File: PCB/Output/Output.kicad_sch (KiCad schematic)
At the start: 44 parts, among them J1 USB-C, J10 O8, J11 O9, J12 O10, J2 POWER, J3 O1, J4 O2, J5 O3, J6 O4, J7 O5, J8 O6, J9 O7, U1 ESP32-PICO-MINI-02, U10 QR, U11 CH340X, U3 ISL89410, U4 ISL89410, U5 ISL89410, U6 ISL89410, U7 ISL89410, U8 MD8942, U9 AA

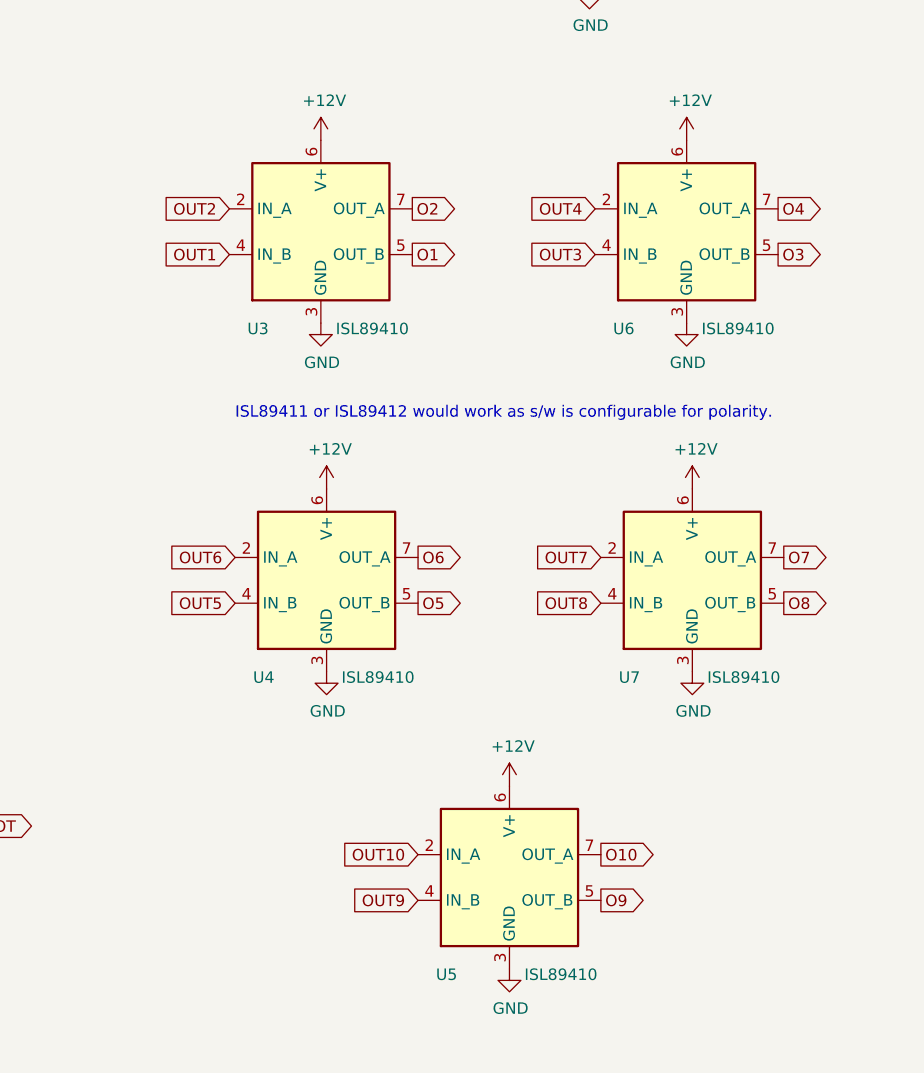
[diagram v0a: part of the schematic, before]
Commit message: Fix output driver
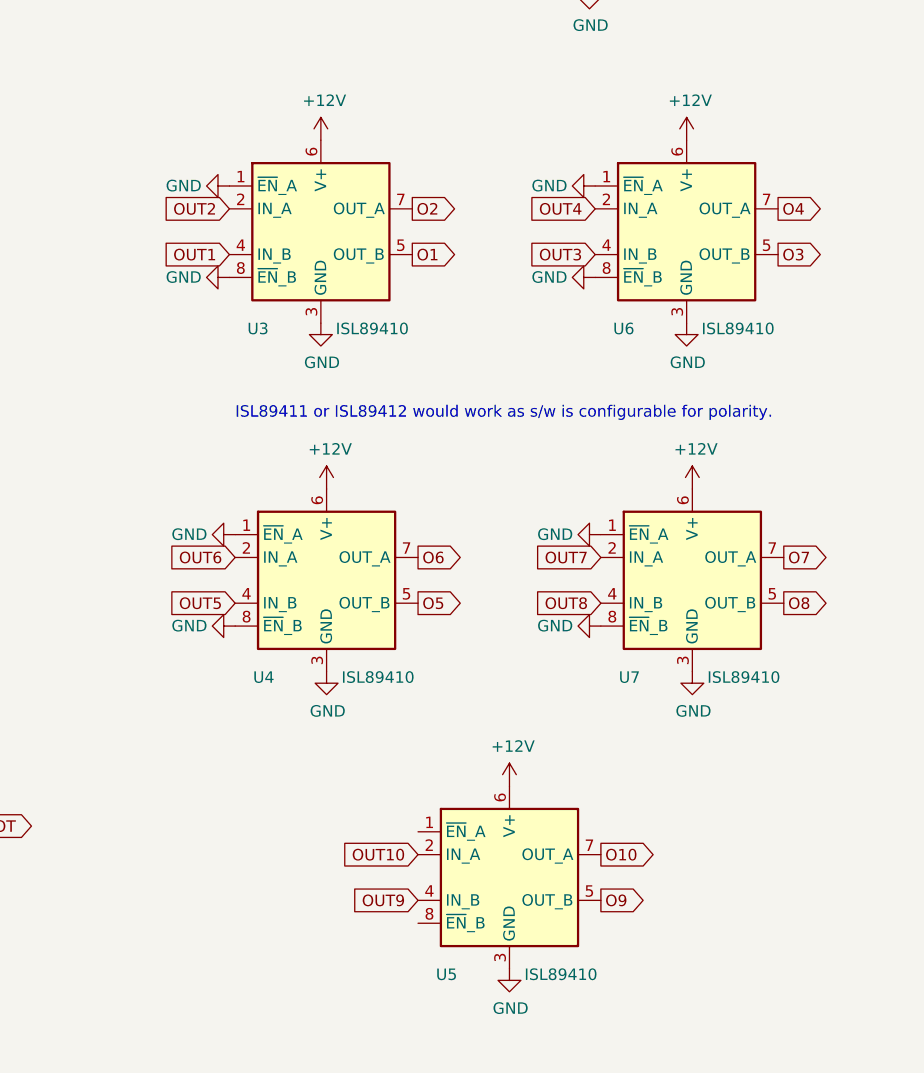
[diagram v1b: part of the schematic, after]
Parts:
- U3, U4, U5, U6, U7: symbol Driver_FET:EL7202CN -> RevK:IVCR2404
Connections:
- net GND: now also U3.1 (~{EN}_A), U3.8 (~{EN}_B), U4.1 (~{EN}_A), U4.8 (~{EN}_B), U6.1 (~{EN}_A), U6.8 (~{EN}_B), U7.1 (~{EN}_A), U7.8 (~{EN}_B)
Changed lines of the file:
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@@
     )
   )
-  (symbol (lib_id "Driver_FET:EL7202CN") (at 113.665 88.265 0) (unit 1)
+  (symbol (lib_id "RevK:IVCR2404") (at 113.665 88.265 0) (unit 1)
     (in_bom yes) (on_board yes) (dnp no)
     (property "Reference" "U3" (at 106.68 99.06 0)
@@
     )
   )
-  (symbol (lib_id "Driver_FET:EL7202CN") (at 154.305 88.265 0) (unit 1)
+  (symbol (lib_id "RevK:IVCR2404") (at 154.305 88.265 0) (unit 1)
     (in_bom yes) (on_board yes) (dnp no)
     (property "Reference" "U6" (at 147.32 99.06 0)
@@
     )
   )
+  (symbol (lib_id "power:GND") (at 144.145 83.185 270) (unit 1)
+    (in_bom yes) (on_board yes) (dnp no)
+    (property "Reference" "#PWR06" (at 137.795 83.185 0)
+      (effects (font (size 1.27 1.27)) hide)
+    )
+    (property "Value" "GND" (at 139.065 83.185 90)
+      (effects (font (size 1.27 1.27)))
+    )
+    (property "Footprint" "" (at 144.145 83.185 0)
+      (effects (font (size 1.27 1.27)) hide)
+    )
+    (property "Datasheet" "" (at 144.145 83.185 0)
+      (effects (font (size 1.27 1.27)) hide)
+    )
+    (pin "1")
+    (instances
+      (project "Output"
+        (path "/770ad51a-7219-4633-b24a-bd20feb0a6c5"
+          (reference "#PWR06") (unit 1)
+        )
+      )
+    )
+  )
   (symbol (lib_id "RevK:Hidden") (at 255.905 30.48 270) (unit 1)
     (in_bom yes) (on_board yes) (dnp no)
@@
     )
   )
+  (symbol (lib_id "power:GND") (at 144.145 93.345 270) (unit 1)
+    (in_bom yes) (on_board yes) (dnp no)
+    (property "Reference" "#PWR07" (at 137.795 93.345 0)
+      (effects (font (size 1.27 1.27)) hide)
+    )
+    (property "Value" "GND" (at 139.065 93.345 90)
+      (effects (font (size 1.27 1.27)))
+    )
+    (property "Footprint" "" (at 144.145 93.345 0)
+      (effects (font (size 1.27 1.27)) hide)
+    )
+    (property "Datasheet" "" (at 144.145 93.345 0)
+      (effects (font (size 1.27 1.27)) hide)
+    )
+    (pin "1")
+    (instances
+      (project "Output"
+        (path "/770ad51a-7219-4633-b24a-bd20feb0a6c5"
+          (reference "#PWR07") (unit 1)
+        )
+      )
+    )
+  )
   (symbol (lib_id "power:GND") (at 154.94 137.16 0) (unit 1)
     (in_bom yes) (on_board yes) (dnp no)
@@
     )
   )
-  (symbol (lib_id "Driver_FET:EL7202CN") (at 134.62 160.02 0) (unit 1)
+  (symbol (lib_id "RevK:IVCR2404") (at 134.62 160.02 0) (unit 1)
     (in_bom yes) (on_board yes) (dnp no)
     (property "Reference" "U5" (at 127.635 170.815 0)
@@
         (path "/770ad51a-7219-4633-b24a-bd20feb0a6c5"
           (reference "#PWR017") (unit 1)
+        )
+      )
+    )
+  )
+  (symbol (lib_id "power:GND") (at 144.78 121.92 270) (unit 1)
+    (in_bom yes) (on_board yes) (dnp no)
+    (property "Reference" "#PWR010" (at 138.43 121.92 0)
+      (effects (font (size 1.27 1.27)) hide)
+    )
+    (property "Value" "GND" (at 139.7 121.92 90)
+      (effects (font (size 1.27 1.27)))
+    )
+    (property "Footprint" "" (at 144.78 121.92 0)
+      (effects (font (size 1.27 1.27)) hide)
+    )
+    (property "Datasheet" "" (at 144.78 121.92 0)
+      (effects (font (size 1.27 1.27)) hide)
+    )
+    (pin "1")
+    (instances
+      (project "Output"
+        (path "/770ad51a-7219-4633-b24a-bd20feb0a6c5"
+          (reference "#PWR010") (unit 1)
         )
       )
@@
     )
   )
+  (symbol (lib_id "power:GND") (at 103.505 93.345 270) (unit 1)
+    (in_bom yes) (on_board yes) (dnp no)
+    (property "Reference" "#PWR03" (at 97.155 93.345 0)
+      (effects (font (size 1.27 1.27)) hide)
+    )
+    (property "Value" "GND" (at 98.425 93.345 90)
+      (effects (font (size 1.27 1.27)))
+    )
+    (property "Footprint" "" (at 103.505 93.345 0)
+      (effects (font (size 1.27 1.27)) hide)
+    )
+    (property "Datasheet" "" (at 103.505 93.345 0)
+      (effects (font (size 1.27 1.27)) hide)
+    )
+    (pin "1")
+    (instances
+      (project "Output"
+        (path "/770ad51a-7219-4633-b24a-bd20feb0a6c5"
+          (reference "#PWR03") (unit 1)
+        )
+      )
+    )
+  )
   (symbol (lib_id "power:GND") (at 134.62 170.18 0) (unit 1)
     (in_bom yes) (on_board yes) (dnp no)
@@
     )
   )
-  (symbol (lib_id "Driver_FET:EL7202CN") (at 154.94 127 0) (unit 1)
+  (symbol (lib_id "RevK:IVCR2404") (at 154.94 127 0) (unit 1)
     (in_bom yes) (on_board yes) (dnp no)
     (property "Reference" "U7" (at 147.955 137.795 0)
@@
     )
   )
+  (symbol (lib_id "power:GND") (at 104.14 121.92 270) (unit 1)
+    (in_bom yes) (on_board yes) (dnp no)
+    (property "Reference" "#PWR08" (at 97.79 121.92 0)
+      (effects (font (size 1.27 1.27)) hide)
+    )
+    (property "Value" "GND" (at 99.06 121.92 90)
+      (effects (font (size 1.27 1.27)))
+    )
+    (property "Footprint" "" (at 104.14 121.92 0)
+      (effects (font (size 1.27 1.27)) hide)
+    )
+    (property "Datasheet" "" (at 104.14 121.92 0)
+      (effects (font (size 1.27 1.27)) hide)
+    )
+    (pin "1")
+    (instances
+      (project "Output"
+        (path "/770ad51a-7219-4633-b24a-bd20feb0a6c5"
+          (reference "#PWR08") (unit 1)
+        )
+      )
+    )
+  )
   (symbol (lib_id "Connector_Generic:Conn_01x02") (at 243.84 142.24 0) (unit 1)
     (in_bom yes) (on_board yes) (dnp no) (fields_autoplaced)
@@
     )
   )
-  (symbol (lib_id "Driver_FET:EL7202CN") (at 114.3 127 0) (unit 1)
+  (symbol (lib_id "RevK:IVCR2404") (at 114.3 127 0) (unit 1)
     (in_bom yes) (on_board yes) (dnp no)
     (property "Reference" "U4" (at 107.315 137.795 0)
@@
     )
   )
+  (symbol (lib_id "power:GND") (at 144.78 132.08 270) (unit 1)
+    (in_bom yes) (on_board yes) (dnp no)
+    (property "Reference" "#PWR011" (at 138.43 132.08 0)
+      (effects (font (size 1.27 1.27)) hide)
+    )
+    (property "Value" "GND" (at 139.7 132.08 90)
+      (effects (font (size 1.27 1.27)))
+    )
+    (property "Footprint" "" (at 144.78 132.08 0)
+      (effects (font (size 1.27 1.27)) hide)
+    )
+    (property "Datasheet" "" (at 144.78 132.08 0)
+      (effects (font (size 1.27 1.27)) hide)
+    )
+    (pin "1")
+    (instances
+      (project "Output"
+        (path "/770ad51a-7219-4633-b24a-bd20feb0a6c5"
+          (reference "#PWR011") (unit 1)
+        )
+      )
+    )
+  )
+  (symbol (lib_id "power:GND") (at 103.505 83.185 270) (unit 1)
+    (in_bom yes) (on_board yes) (dnp no)
+    (property "Reference" "#PWR04" (at 97.155 83.185 0)
+      (effects (font (size 1.27 1.27)) hide)
+    )
+    (property "Value" "GND" (at 98.425 83.185 90)
+      (effects (font (size 1.27 1.27)))
+    )
+    (property "Footprint" "" (at 103.505 83.185 0)
+      (effects (font (size 1.27 1.27)) hide)
+    )
+    (property "Datasheet" "" (at 103.505 83.185 0)
+      (effects (font (size 1.27 1.27)) hide)
+    )
+    (pin "1")
+    (instances
+      (project "Output"
+        (path "/770ad51a-7219-4633-b24a-bd20feb0a6c5"
+          (reference "#PWR04") (unit 1)
+        )
+      )
+    )
+  )
   (symbol (lib_id "power:GND") (at 66.04 52.07 90) (unit 1)
     (in_bom yes) (on_board yes) (dnp no) (fields_autoplaced)
@@
         )
       )
+    )
+  )
+  (symbol (lib_id "power:GND") (at 104.14 132.08 270) (unit 1)
+    (in_bom yes) (on_board yes) (dnp no)
+    (property "Reference" "#PWR09" (at 97.79 132.08 0)
+      (effects (font (size 1.27 1.27)) hide)
+    )
+    (property "Value" "GND" (at 99.06 132.08 90)
+      (effects (font (size 1.27 1.27)))
+    )
+    (property "Footprint" "" (at 104.14 132.08 0)
+      (effects (font (size 1.27 1.27)) hide)
+    )
+    (property "Datasheet" "" (at 104.14 132.08 0)
+      (effects (font (size 1.27 1.27)) hide)
+    )
+    (pin "1")
+    (instances
+      (project "Output"
+        (path "/770ad51a-7219-4633-b24a-bd20feb0a6c5"
+          (reference "#PWR09") (unit 1)
+        )
+      )

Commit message: Driver
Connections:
- net GND: no longer U3.1 (~{EN}_A), U3.8 (~{EN}_B), U4.1 (~{EN}_A), U4.8 (~{EN}_B), U6.1 (~{EN}_A), U6.8 (~{EN}_B), U7.1 (~{EN}_A), U7.8 (~{EN}_B)
- no-connect marks 10 -> 20
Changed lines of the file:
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@@
   (junction (at 137.16 29.21) (diameter 0) (color 0 0 0 0)
   )
+  (no_connect (at 104.14 121.92))
   (no_connect (at 223.52 34.29))
+  (no_connect (at 144.145 93.345))
+  (no_connect (at 124.46 154.94))
+  (no_connect (at 144.78 132.08))
   (no_connect (at 35.56 66.04))
   (no_connect (at 35.56 60.96))
@@
   (no_connect (at 35.56 40.64))
   (no_connect (at 35.56 43.18))
+  (no_connect (at 144.78 121.92))
+  (no_connect (at 104.14 132.08))
+  (no_connect (at 103.505 93.345))
+  (no_connect (at 124.46 165.1))
+  (no_connect (at 103.505 83.185))
+  (no_connect (at 144.145 83.185))
   (wire (pts (xy 127 30.48) (xy 129.54 30.48))
     (stroke (width 0) (type default))
@@
     )
   )
-  (symbol (lib_id "power:GND") (at 144.145 83.185 270) (unit 1)
-    (in_bom yes) (on_board yes) (dnp no)
-    (property "Reference" "#PWR06" (at 137.795 83.185 0)
-      (effects (font (size 1.27 1.27)) hide)
-    )
-    (property "Value" "GND" (at 139.065 83.185 90)
-      (effects (font (size 1.27 1.27)))
-    )
-    (property "Footprint" "" (at 144.145 83.185 0)
-      (effects (font (size 1.27 1.27)) hide)
-    )
-    (property "Datasheet" "" (at 144.145 83.185 0)
-      (effects (font (size 1.27 1.27)) hide)
-    )
-    (pin "1")
-    (instances
-      (project "Output"
-        (path "/770ad51a-7219-4633-b24a-bd20feb0a6c5"
-          (reference "#PWR06") (unit 1)
-        )
-      )
-    )
-  )
   (symbol (lib_id "RevK:Hidden") (at 255.905 30.48 270) (unit 1)
     (in_bom yes) (on_board yes) (dnp no)
@@
         (path "/825c70b0-4860-42b7-97dc-86bfa46e06fd"
           (reference "V2") (unit 1)
-        )
-      )
-    )
-  )
-  (symbol (lib_id "power:GND") (at 144.145 93.345 270) (unit 1)
-    (in_bom yes) (on_board yes) (dnp no)
-    (property "Reference" "#PWR07" (at 137.795 93.345 0)
-      (effects (font (size 1.27 1.27)) hide)
-    )
-    (property "Value" "GND" (at 139.065 93.345 90)
-      (effects (font (size 1.27 1.27)))
-    )
-    (property "Footprint" "" (at 144.145 93.345 0)
-      (effects (font (size 1.27 1.27)) hide)
-    )
-    (property "Datasheet" "" (at 144.145 93.345 0)
-      (effects (font (size 1.27 1.27)) hide)
-    )
-    (pin "1")
-    (instances
-      (project "Output"
-        (path "/770ad51a-7219-4633-b24a-bd20feb0a6c5"
-          (reference "#PWR07") (unit 1)
         )
       )
@@
         (path "/770ad51a-7219-4633-b24a-bd20feb0a6c5"
           (reference "#PWR017") (unit 1)
-        )
-      )
-    )
-  )
-  (symbol (lib_id "power:GND") (at 144.78 121.92 270) (unit 1)
-    (in_bom yes) (on_board yes) (dnp no)
-    (property "Reference" "#PWR010" (at 138.43 121.92 0)
-      (effects (font (size 1.27 1.27)) hide)
-    )
-    (property "Value" "GND" (at 139.7 121.92 90)
-      (effects (font (size 1.27 1.27)))
-    )
-    (property "Footprint" "" (at 144.78 121.92 0)
-      (effects (font (size 1.27 1.27)) hide)
-    )
-    (property "Datasheet" "" (at 144.78 121.92 0)
-      (effects (font (size 1.27 1.27)) hide)
-    )
-    (pin "1")
-    (instances
-      (project "Output"
-        (path "/770ad51a-7219-4633-b24a-bd20feb0a6c5"
-          (reference "#PWR010") (unit 1)
         )
       )
@@
     )
   )
-  (symbol (lib_id "power:GND") (at 103.505 93.345 270) (unit 1)
-    (in_bom yes) (on_board yes) (dnp no)
-    (property "Reference" "#PWR03" (at 97.155 93.345 0)
-      (effects (font (size 1.27 1.27)) hide)
-    )
-    (property "Value" "GND" (at 98.425 93.345 90)
-      (effects (font (size 1.27 1.27)))
-    )
-    (property "Footprint" "" (at 103.505 93.345 0)
-      (effects (font (size 1.27 1.27)) hide)
-    )
-    (property "Datasheet" "" (at 103.505 93.345 0)
-      (effects (font (size 1.27 1.27)) hide)
-    )
-    (pin "1")
-    (instances
-      (project "Output"
-        (path "/770ad51a-7219-4633-b24a-bd20feb0a6c5"
-          (reference "#PWR03") (unit 1)
-        )
-      )
-    )
-  )
   (symbol (lib_id "power:GND") (at 134.62 170.18 0) (unit 1)
     (in_bom yes) (on_board yes) (dnp no)
@@
     )
   )
-  (symbol (lib_id "power:GND") (at 104.14 121.92 270) (unit 1)
-    (in_bom yes) (on_board yes) (dnp no)
-    (property "Reference" "#PWR08" (at 97.79 121.92 0)
-      (effects (font (size 1.27 1.27)) hide)
-    )
-    (property "Value" "GND" (at 99.06 121.92 90)
-      (effects (font (size 1.27 1.27)))
-    )
-    (property "Footprint" "" (at 104.14 121.92 0)
-      (effects (font (size 1.27 1.27)) hide)
-    )
-    (property "Datasheet" "" (at 104.14 121.92 0)
-      (effects (font (size 1.27 1.27)) hide)
-    )
-    (pin "1")
-    (instances
-      (project "Output"
-        (path "/770ad51a-7219-4633-b24a-bd20feb0a6c5"
-          (reference "#PWR08") (unit 1)
-        )
-      )
-    )
-  )
   (symbol (lib_id "Connector_Generic:Conn_01x02") (at 243.84 142.24 0) (unit 1)
     (in_bom yes) (on_board yes) (dnp no) (fields_autoplaced)
@@
     )
   )
-  (symbol (lib_id "power:GND") (at 144.78 132.08 270) (unit 1)
-    (in_bom yes) (on_board yes) (dnp no)
-    (property "Reference" "#PWR011" (at 138.43 132.08 0)
-      (effects (font (size 1.27 1.27)) hide)
-    )
-    (property "Value" "GND" (at 139.7 132.08 90)
-      (effects (font (size 1.27 1.27)))
-    )
-    (property "Footprint" "" (at 144.78 132.08 0)
-      (effects (font (size 1.27 1.27)) hide)
-    )
-    (property "Datasheet" "" (at 144.78 132.08 0)
-      (effects (font (size 1.27 1.27)) hide)
-    )
-    (pin "1")
-    (instances
-      (project "Output"
-        (path "/770ad51a-7219-4633-b24a-bd20feb0a6c5"
-          (reference "#PWR011") (unit 1)
-        )
-      )
-    )
-  )
-  (symbol (lib_id "power:GND") (at 103.505 83.185 270) (unit 1)
-    (in_bom yes) (on_board yes) (dnp no)
-    (property "Reference" "#PWR04" (at 97.155 83.185 0)
-      (effects (font (size 1.27 1.27)) hide)
-    )
-    (property "Value" "GND" (at 98.425 83.185 90)
-      (effects (font (size 1.27 1.27)))
-    )
-    (property "Footprint" "" (at 103.505 83.185 0)
-      (effects (font (size 1.27 1.27)) hide)
-    )
-    (property "Datasheet" "" (at 103.505 83.185 0)
-      (effects (font (size 1.27 1.27)) hide)
-    )
-    (pin "1")
-    (instances
-      (project "Output"
-        (path "/770ad51a-7219-4633-b24a-bd20feb0a6c5"
-          (reference "#PWR04") (unit 1)
-        )
-      )
-    )
-  )
   (symbol (lib_id "power:GND") (at 66.04 52.07 90) (unit 1)
     (in_bom yes) (on_board yes) (dnp no) (fields_autoplaced)
@@
         )
       )
-    )
-  )
-  (symbol (lib_id "power:GND") (at 104.14 132.08 270) (unit 1)
-    (in_bom yes) (on_board yes) (dnp no)
-    (property "Reference" "#PWR09" (at 97.79 132.08 0)
-      (effects (font (size 1.27 1.27)) hide)
-    )
-    (property "Value" "GND" (at 99.06 132.08 90)
-      (effects (font (size 1.27 1.27)))
-    )
-    (property "Footprint" "" (at 104.14 132.08 0)
-      (effects (font (size 1.27 1.27)) hide)
-    )
-    (property "Datasheet" "" (at 104.14 132.08 0)
-      (effects (font (size 1.27 1.27)) hide)
-    )
-    (pin "1")
-    (instances
-      (project "Output"
-        (path "/770ad51a-7219-4633-b24a-bd20feb0a6c5"
-          (reference "#PWR09") (unit 1)
-        )
-      )

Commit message: ESP32-S3
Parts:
- removed C1: 0.1uF, RevK:C_0402, symbol Device:C
- removed D1: RGB, RevK:LED-RGB-1.6x1.6, symbol Device:LED_RGBA
- removed D2: D, RevK:D_1206, symbol Device:D
- removed R2: 2K, RevK:R_0402, symbol Device:R
- removed R3: 220R, RevK:R_0402, symbol Device:R
- removed U1: ESP32-PICO-MINI-02, RevK:ESP32-PICO-MINI-02, symbol RevK:ESP32-PICO-MINI-02
- removed U10: QR, RevK:QR-SS, symbol RevK:QR
- removed U11: CH340X, RevK:CH340X, symbol RevK:CH340X
- removed U9: AA, RevK:AA, symbol RevK:AA
- added C1 (x12): 100nF, RevK:C_0402, symbol Device:C
- added C3: 1uF, RevK:C_0402, symbol Device:C
- added D1 (x11): XL-1010RGBC-WS2812B, RevK:SMD1010, symbol RevK:WS2812B-1mm
- added D3: D, RevK:D_SOD-123, symbol Device:D
- added J2: Shelly, RevK:Shelly, symbol RevK:Shelly
- added U2: ESP32-S3-MINI-1, RevK:ESP32-S3-MINI-1, symbol RevK:ESP32-S3-MINI-1-N4R2
- C2: value 0.1uF -> 22uF
- J1: renamed from J2; now left out of the parts list
- J10: renamed from J9; now left out of the parts list
- J11: renamed from J10; now left out of the parts list
- J12: renamed from J11; now left out of the parts list
- J13: renamed from J12; now left out of the parts list
- J4: renamed from J3; now left out of the parts list
- J5: renamed from J4; now left out of the parts list
- J6: renamed from J5; now left out of the parts list
- J7: renamed from J6; now left out of the parts list
- J8: renamed from J7; now left out of the parts list
- J9: renamed from J8; now left out of the parts list
- R1: value 680R -> 10K
- V1: footprint RevK:VCUT70 -> RevK:VCUT70N
- V2: renamed from V3; footprint RevK:VCUT70 -> RevK:VCUT70N
- V3: renamed from V4; footprint RevK:VCUT70 -> RevK:VCUT70N
- V4: renamed from V2; footprint RevK:VCUT70 -> RevK:VCUT70N
- renumbered C3 to C1, C4 to C2, C9 to C3, J1 to J2, R4 to R1, R16 to R2, R5 to R3, R17 to R4, R18 to R5, U8 to U1, U6 to U4, U4 to U5, U7 to U6, U5 to U7
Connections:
- net +12V: now also D3.1 (K)
- net +3.3V: now also R1.1, C1.1, C1.1, C1.1, C1.1, C1.1, C1.1, C1.1, C1.1, C1.1, C1.1, C1.1, C1.1, D1.2 (+), D1.2 (+), D1.2 (+), D1.2 (+), D1.2 (+), D1.2 (+), D1.2 (+), D1.2 (+), D1.2 (+), D1.2 (+), D1.2 (+), J2.3 (3V3), U2.3 (3V3)
- net D+: now also U2.24 (GPIO20)
- net D-: now also U2.23 (GPIO19)
- net GND: now also C1.2, C1.2, C1.2, C1.2, C1.2, C1.2, C1.2, C1.2, C1.2, C1.2, C1.2, C1.2, C3.2, D1.3 (⏚), D1.3 (⏚), D1.3 (⏚), D1.3 (⏚), D1.3 (⏚), D1.3 (⏚), D1.3 (⏚), D1.3 (⏚), D1.3 (⏚), D1.3 (⏚), D1.3 (⏚), J2.1 (GND), U2.1 (GND), U2.2 (GND), U2.42 (GND), U2.43 (GND), U2.46 (GND), U2.47 (GND), U2.48 (GND), U2.49 (GND), U2.50 (GND), U2.51 (GND), U2.52 (GND), U2.53 (GND), U2.54 (GND), U2.55 (GND), U2.56 (GND), U2.57 (GND), U2.58 (GND), U2.59 (GND), U2.60 (GND), U2.61 (GND), U2.62 (GND), U2.63 (GND), U2.64 (GND), U2.65 (GND)
- net O1: now also U3.7 (OUT_A); no longer U3.5 (OUT_B)
- net O10: now also U7.5 (OUT_B); no longer U7.7 (OUT_A)
- net O2: now also U3.5 (OUT_B); no longer U3.7 (OUT_A)
- net O3: now also U4.7 (OUT_A); no longer U4.5 (OUT_B)
- net O4: now also U4.5 (OUT_B); no longer U4.7 (OUT_A)
- net O9: now also U7.7 (OUT_A); no longer U7.5 (OUT_B)
- net OUT1: now also U3.2 (IN_A), U2.10 (GPIO6); no longer U3.4 (IN_B)
- net OUT10: now also U7.4 (IN_B), U2.37 (GPIO41); no longer U7.2 (IN_A)
- net OUT2: now also U3.4 (IN_B), U2.8 (GPIO4); no longer U3.2 (IN_A)
- net OUT3: now also U4.2 (IN_A), U2.17 (GPIO13); no longer U4.4 (IN_B)
- net OUT4: now also U4.4 (IN_B), U2.19 (GPIO15); no longer U4.2 (IN_A)
- net OUT5: now also U2.27 (GPIO47)
- net OUT6: now also U2.28 (GPIO33)
- net OUT7: now also U2.32 (GPIO36)
- net OUT8: now also U2.34 (GPIO38)
- net OUT9: now also U7.2 (IN_A), U2.38 (GPIO42); no longer U7.4 (IN_B)
- net VBUS: now also D3.2 (A)
- net R: no longer names the net of R1.2
- net R: now also C3.1, U2.45 (EN)
- new net: D1.1 (O), D1.4 (I) (x10)
- new net: J2.2 (0), U2.4 (GPIO0)
- new net: J2.4 (Rx), U2.40 (GPIO44)
- new net: J2.5 (Tx), U2.39 (GPIO43)
- new net RGB: D1.4 (I), U2.21 (GPIO17)
- no-connect marks 20 -> 34
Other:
- moved on the sheet: J10, J11, J12, J13, J2, J4, J5, J6, J7, J8, J9, R1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
